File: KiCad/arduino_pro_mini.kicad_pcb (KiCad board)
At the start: 4 copper layers, 25 x 42.5 mm, 27 parts, among them IC101 UA78M05CDCYR, IC102 ATMEGA328P-AU, J101 Conn_01x06_Pin, J102 Conn_01x15_Pin, J103 Conn_01x15_Pin, J104 Conn_02x03_Odd_Even, SW101 SW_Omron_B3FS, Y101 16Mhz

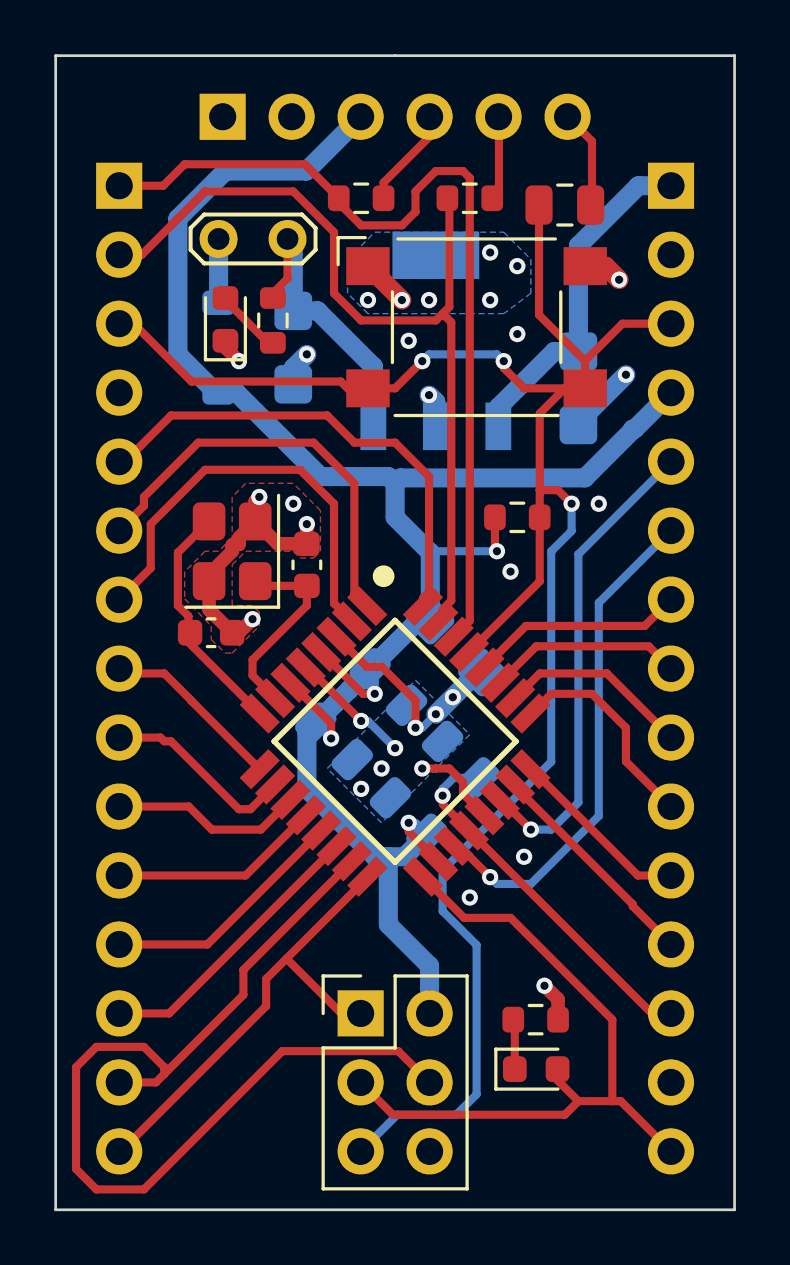
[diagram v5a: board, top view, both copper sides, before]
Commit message: silk screen updates
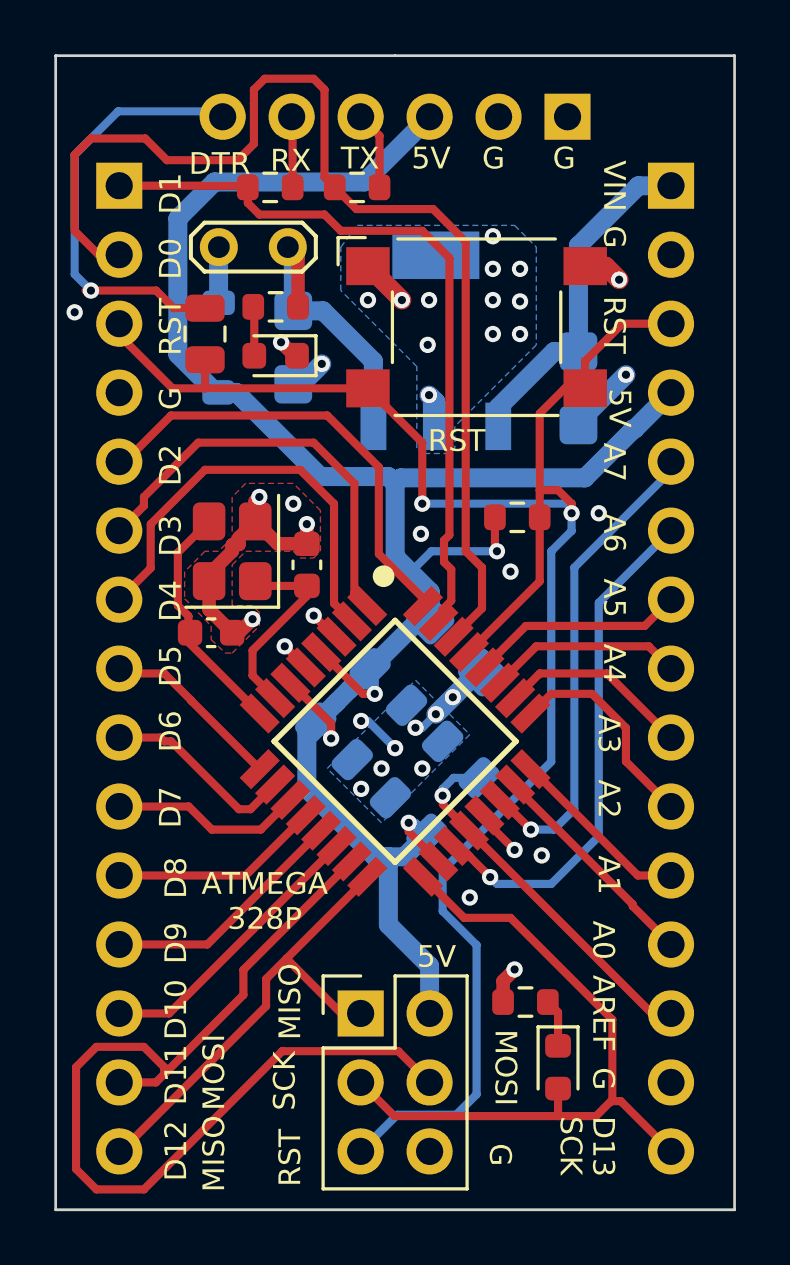
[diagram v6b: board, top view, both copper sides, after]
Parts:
- moved C110 14.1 mm to (43.0, 58.0), turned to 90 degrees
- moved J101 12.7 mm to (56.4, 50.0), turned to 90 degrees
- moved R103 7.36 mm to (45.4, 52.6)
- moved D102 2.28 mm to (45.6, 58.8), turned to 180 degrees
- moved D103 0.81 mm to (56.0, 85.0), turned to -90 degrees
- moved R105 0.75 mm to (54.8, 82.6), turned to 180 degrees
- moved R101 0.51 mm to (45.6, 57.0), turned to 180 degrees
- moved R102 0.43 mm to (48.6, 52.6)
- moved JP101 0.30 mm to (46.0, 54.8)
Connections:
- J102 pad 1: D0_RX -> D1_TX
- J102 pad 2: D1_TX -> D0_RX
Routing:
- net /DTR: track 3.71 -> 16.1 mm, vias 0 -> 1
- net D0_RX: track 33.4 -> 41.8 mm
- net GND: track 36.9 -> 29.8 mm, vias 30 -> 38
- net D1_TX: track 32.4 -> 28.0 mm
- net +5V: track 74.5 -> 78.8 mm
- net RESET: track 73.5 -> 70.0 mm, vias 3 -> 2
- net D2: track 17.9 -> 16.8 mm
- net /TXD: track 3.70 -> 2.89 mm
- net Net-(D102-A): track 2.48 -> 1.76 mm
- net +5V_LDO: track 11.1 -> 11.8 mm
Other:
- board text added: "5V"
- board text added: "A0"
- board text added: "A1"
- board text added: "A2"
- board text added: "A3"
- board text added: "A4"
- board text added: "A5"
- board text added: "A6"
- board text added: "A7"
- board text added: "AREF"
- board text added: "ATMEGA 328P"
- board text added: "D0"
- board text added: "D1"
- board text added: "D10"
- board text added: "D11"
- board text added: "D12"
- board text added: "D13"
- board text added: "D2"
- board text added: "D3"
- board text added: "D4"
- board text added: "D5"
- board text added: "D6"
- board text added: "D7"
- board text added: "D8"
- board text added: "D9"
- board text added: "DTR"
- board text added: "G"
- board text added: "MISO"
- board text added: "MOSI"
- board text added: "RST"
- board text added: "RX"
- board text added: "SCK"
- board text added: "TX"
- board text added: "VIN"

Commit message: UART signals routing update
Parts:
- moved C105 1.60 mm to (56.8, 58.4)
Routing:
- net D0_RX: track 41.8 -> 46.0 mm
- net D1_TX: track 28.0 -> 32.2 mm
- net GND: track 29.8 -> 29.7 mm, vias 38 -> 59
